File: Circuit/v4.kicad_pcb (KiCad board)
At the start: 2 copper layers, 30 x 50 mm, 52 parts, among them J2 AVR-ISP-6, Q1 AO3400A, U1 EL3H7(B)(TA)-G

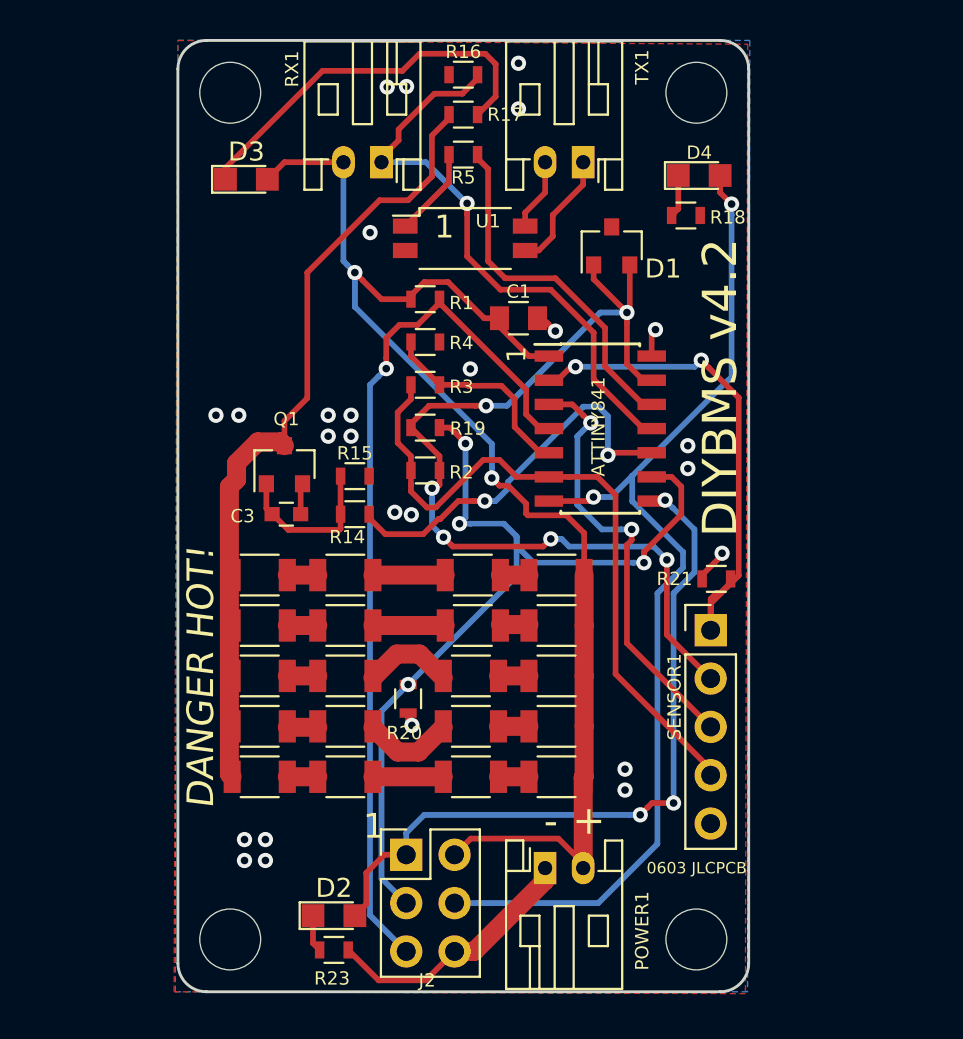
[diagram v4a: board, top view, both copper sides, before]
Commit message: Increased size of ground/negative connection to MOSFET
Thank you to George Boudreau for highlighting
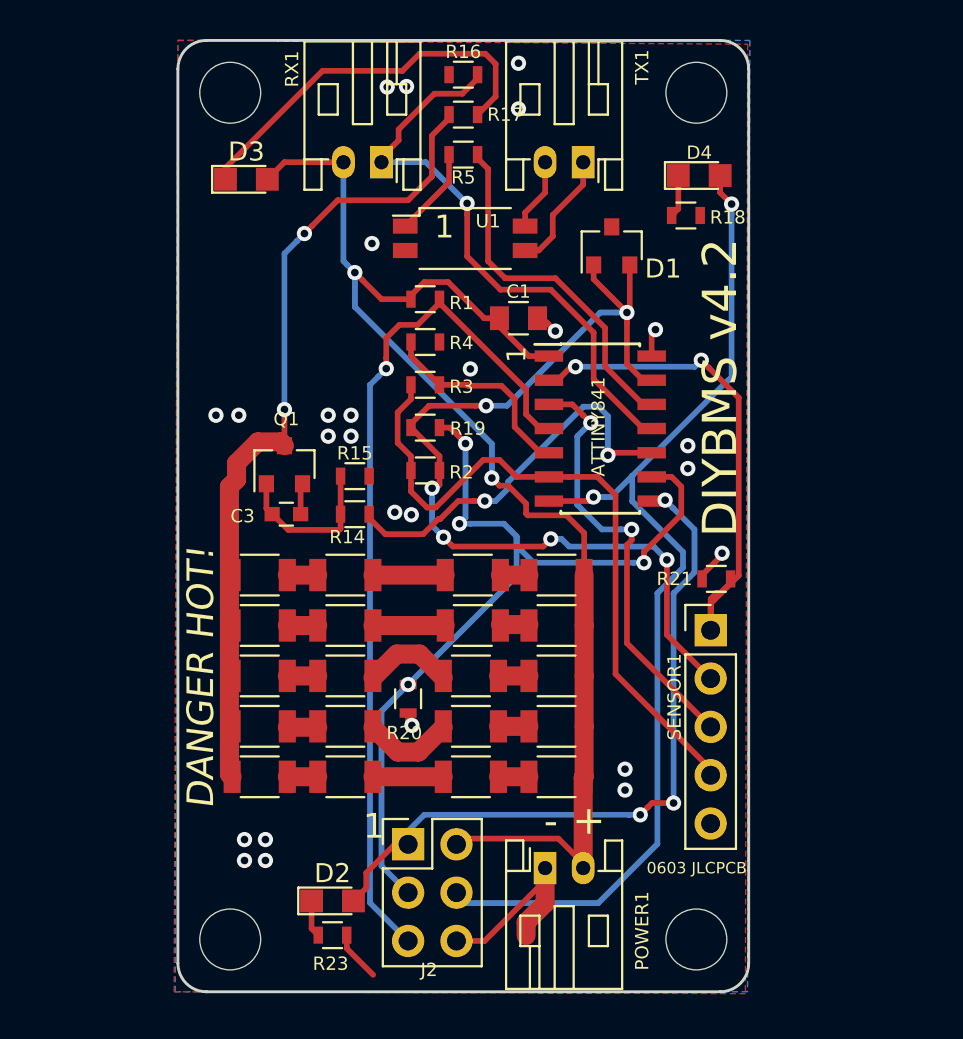
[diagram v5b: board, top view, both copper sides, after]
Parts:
- moved D2 0.78 mm to (110.0, 93.2)
- moved R23 0.78 mm to (110.0, 95.0)
- moved J2 0.56 mm to (114.0, 90.2)
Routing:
- net Net-(Q1-Pad3): track 41.6 -> 42.9 mm, vias 0 -> 2
- net Net-(ATTINY841-Pad8): track 38.6 -> 37.6 mm
- net GND: track 20.9 -> 20.4 mm
- net Net-(ATTINY841-Pad4): track 46.4 -> 45.9 mm
- net Net-(ATTINY841-Pad9): track 46.2 -> 45.7 mm
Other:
- board text added: "25 Jan 2020"
- board text removed: "6 Jan 2020"

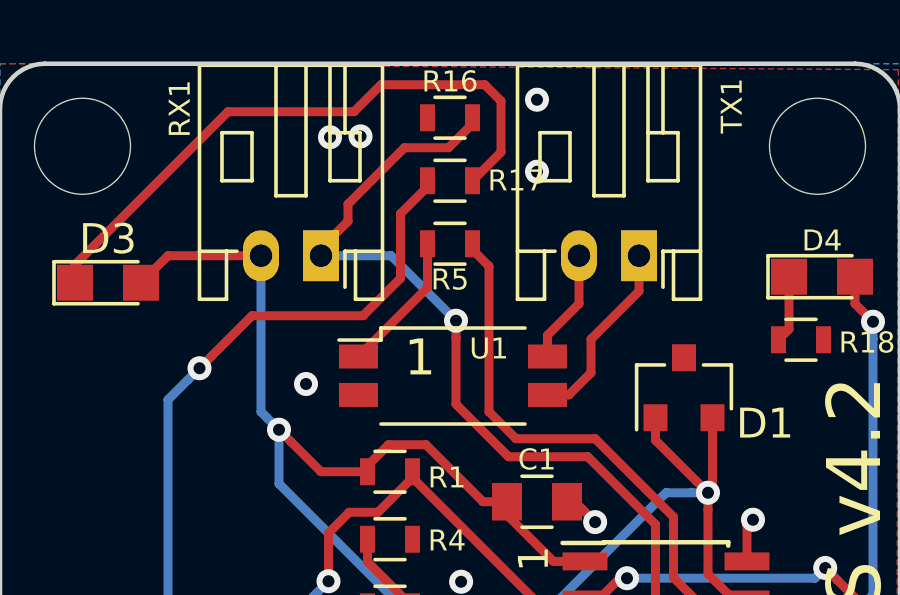
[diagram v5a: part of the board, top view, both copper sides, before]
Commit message: Change R5 to 220ohm instead of 510ohm
Change R5 to 220ohm instead of 510ohm to improve current to optoisolator
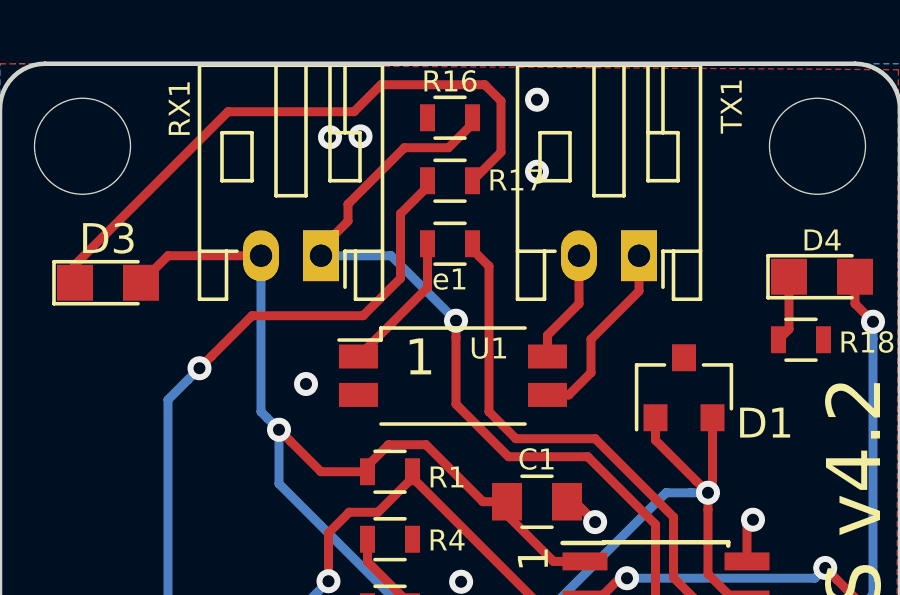
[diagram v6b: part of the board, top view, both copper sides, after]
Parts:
- e1: renamed from R5; value 510OHMS -> 220OHMS

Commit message: Updated R5 to 220ohm
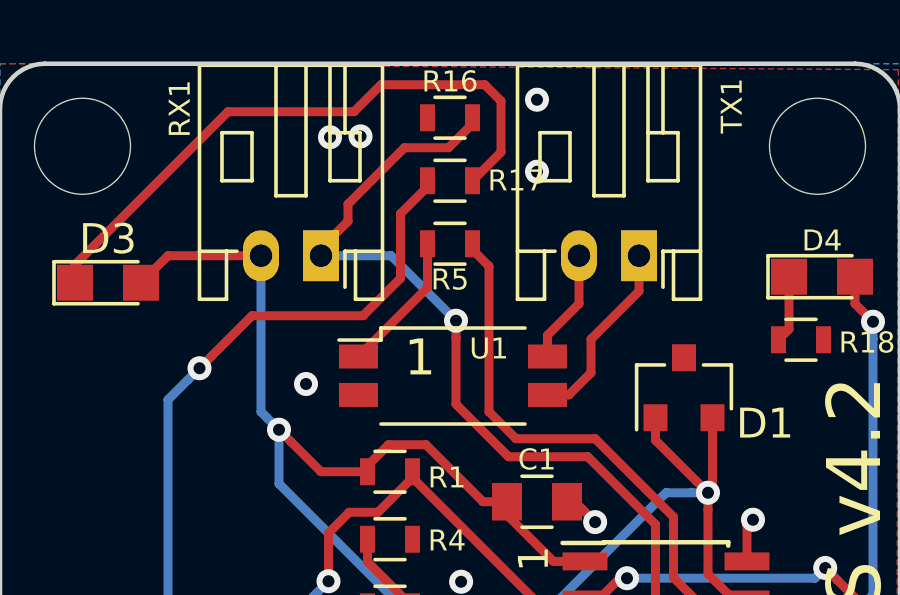
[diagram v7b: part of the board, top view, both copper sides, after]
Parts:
- renumbered e1 to R5
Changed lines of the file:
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@@
   (net 35 "Net-(R32-Pad2)")
   (net 36 "Net-(R33-Pad2)")
-  (net 37 "Net-(U1-Pad1)")
+  (net 37 "Net-(R5-Pad1)")
   (net_class Default "This is the default net class."
     (clearance 0.3)
@@
     (add_net "Net-(R32-Pad2)")
     (add_net "Net-(R33-Pad2)")
+    (add_net "Net-(R5-Pad1)")
     (add_net "Net-(TX1-Pad1)")
     (add_net "Net-(TX1-Pad2)")
-    (add_net "Net-(U1-Pad1)")
     (add_net RXD0)
     (add_net TXD0)
@@
     (fp_line (start 4.05 1.66) (end -4.05 1.66) (layer F.CrtYd) (width 0.05))
     (pad 1 smd rect (at -3.15 -0.64) (size 1.3 0.8) (layers F.Cu F.Paste F.Mask)
-      (net 37 "Net-(U1-Pad1)"))
+      (net 37 "Net-(R5-Pad1)"))
     (pad 2 smd rect (at -3.15 0.64) (size 1.3 0.8) (layers F.Cu F.Paste F.Mask)
       (net 1 GND))
@@
     (tags "resistor 0603")
     (attr smd)
-    (fp_text reference e1 (at 0 1.2) (layer F.SilkS)
+    (fp_text reference R5 (at 0 1.2) (layer F.SilkS)
       (effects (font (size 0.7 0.7) (thickness 0.1)))
     )
@@
     (fp_line (start 1.25 0.7) (end -1.25 0.7) (layer F.CrtYd) (width 0.05))
     (pad 1 smd rect (at -0.75 0) (size 0.5 0.9) (layers F.Cu F.Paste F.Mask)
-      (net 37 "Net-(U1-Pad1)"))
+      (net 37 "Net-(R5-Pad1)"))
     (pad 2 smd rect (at 0.75 0) (size 0.5 0.9) (layers F.Cu F.Paste F.Mask)
       (net 5 TXD0))
@@
   (segment (start 121.4176 70.9276) (end 119.715604 70.9276) (width 0.3) (layer F.Cu) (net 4))
   (segment (start 114.1676 71.3376) (end 114.1676 70.5876) (width 0.3) (layer F.Cu) (net 4))
-  (segment (start 116.1676 55.4476) (end 113.8676 57.7476) (width 0.3) (layer F.Cu) (net 37) (status 20))
-  (segment (start 116.1676 53.9876) (end 116.1676 55.4476) (width 0.3) (layer F.Cu) (net 37) (status 10))
   (segment (start 117.6676 54.1876) (end 117.6676 53.9876) (width 0.3) (layer F.Cu) (net 5))
   (segment (start 118.2176 59.5876) (end 118.2176 54.7376) (width 0.3) (layer F.Cu) (net 5))
@@
   (segment (start 112.1676 76.0876) (end 115.9676 76.0876) (width 1) (layer F.Cu) (net 35))
   (segment (start 107.6676 76.0876) (end 109.2676 76.0876) (width 1) (layer F.Cu) (net 36))
+  (segment (start 116.1676 55.4476) (end 113.8676 57.7476) (width 0.3) (layer F.Cu) (net 37) (status 20))
+  (segment (start 116.1676 53.9876) (end 116.1676 55.4476) (width 0.3) (layer F.Cu) (net 37) (status 10))
   (zone (net 1) (net_name GND) (layer B.Cu) (hatch edge 0.508)
     (connect_pads (clearance 0.508))

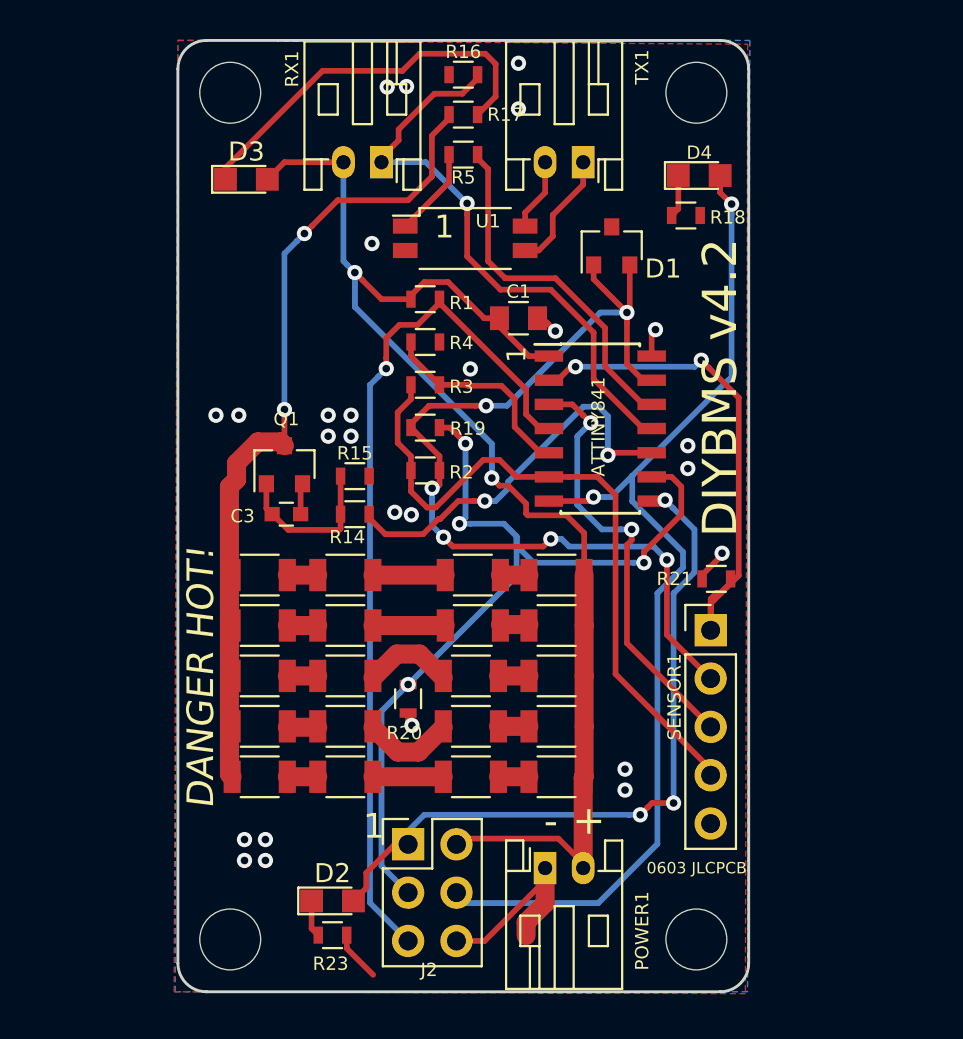
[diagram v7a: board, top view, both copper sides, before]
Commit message: Fix for issue #34
Resolve issue for R19 and R20 being in wrong places
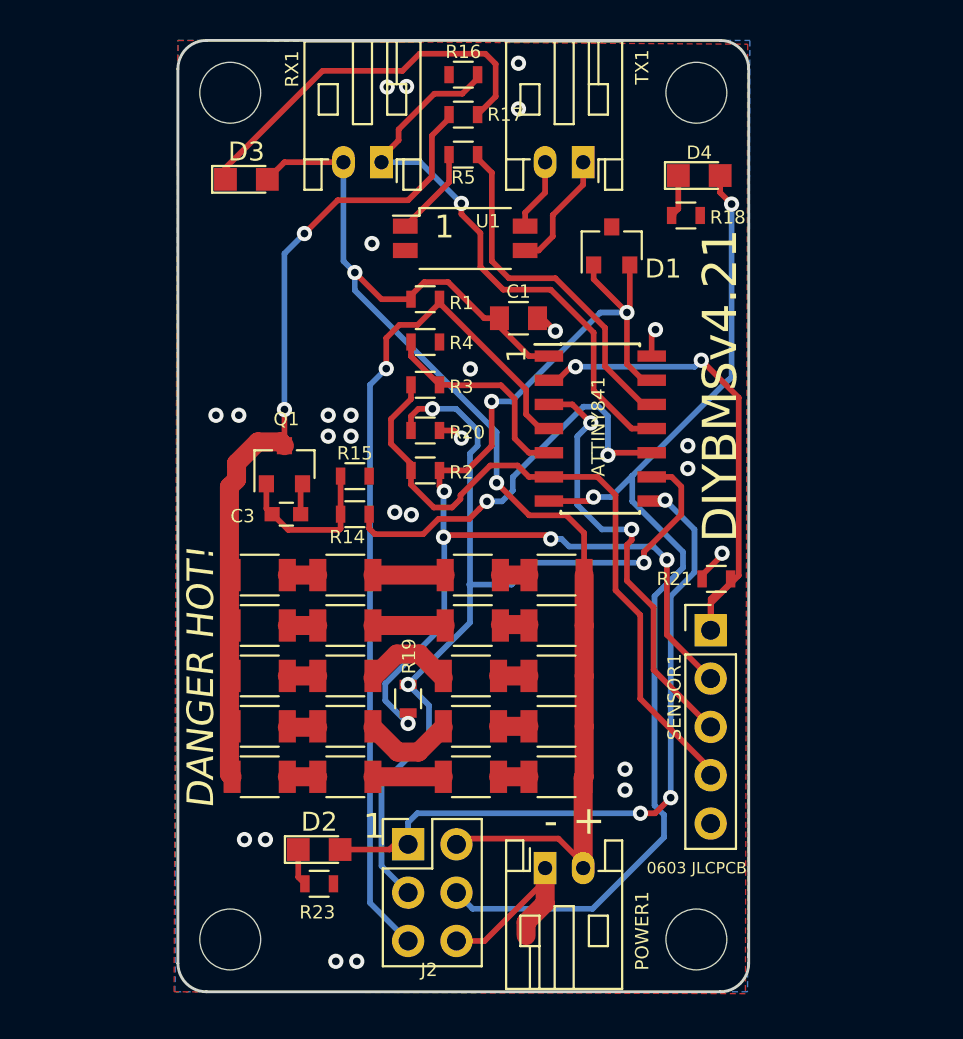
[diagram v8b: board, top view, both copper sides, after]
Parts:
- moved R19 14.3 mm to (114.0, 82.6), turned to 90 degrees
- moved R20 14.1 mm to (114.9, 68.5), turned to 0 degrees
- moved R23 2.79 mm to (109.3, 92.3)
- moved D2 2.79 mm to (109.3, 90.5)
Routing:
- net 2_VOLT: track 50.8 -> 60.1 mm, vias 6 -> 7
- net Net-(ATTINY841-Pad9): track 45.7 -> 49.0 mm, vias 4 -> 3
- net GND: track 20.4 -> 18.0 mm
- net Net-(ATTINY841-Pad8): track 37.6 -> 36.7 mm
- net Net-(ATTINY841-Pad7): track 56.2 -> 56.9 mm
- net DUMP_LOAD_ENABLE: track 20.7 -> 21.2 mm
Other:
- board text added: "24 March 2020"
- board text added: "DIYBMSv4.21"
- board text removed: "25 Jan 2020"
- board text removed: "DIYBMS v4.2"
